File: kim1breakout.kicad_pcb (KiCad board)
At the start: 2 copper layers, 110 x 90.7 mm, 3 parts, among them J1 Conn_01x44, J2 Conn_01x44, J3 Conn_02x22_Top_Bottom

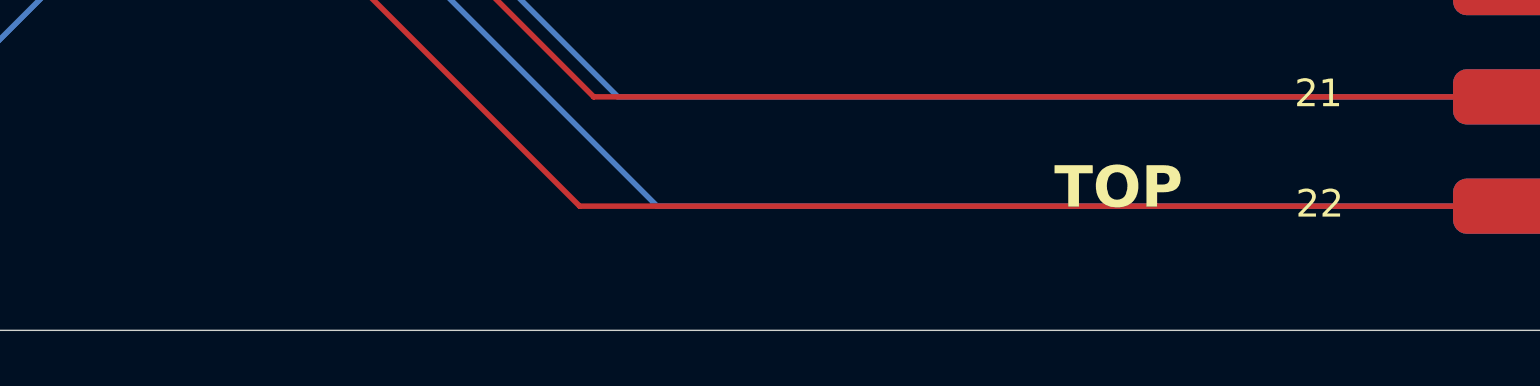
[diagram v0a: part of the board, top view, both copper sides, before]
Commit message: Add pointer to Github repo to the PCB
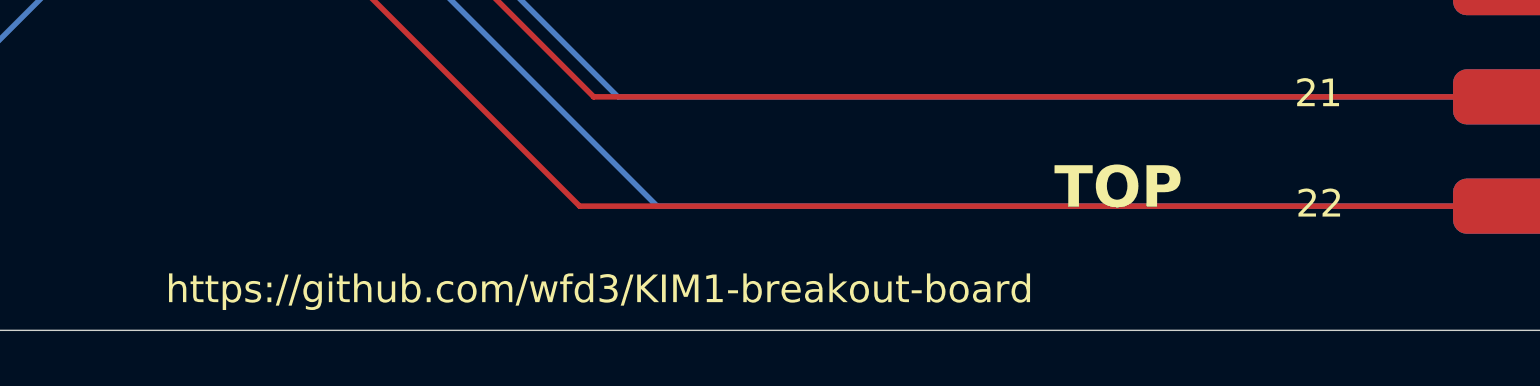
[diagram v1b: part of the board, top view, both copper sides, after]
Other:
- board text added: "https://github.com/wfd3/KIM1-breakout-board"
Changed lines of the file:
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@@
+		)
+	)
+	(gr_text "https://github.com/wfd3/KIM1-breakout-board"
+		(at 153.5 143.5 0)
+		(layer "F.SilkS")
+		(effects
+			(font
+				(size 1 1)
+				(thickness 0.1)
+			)
+			(justify left bottom)
 		)
 	)

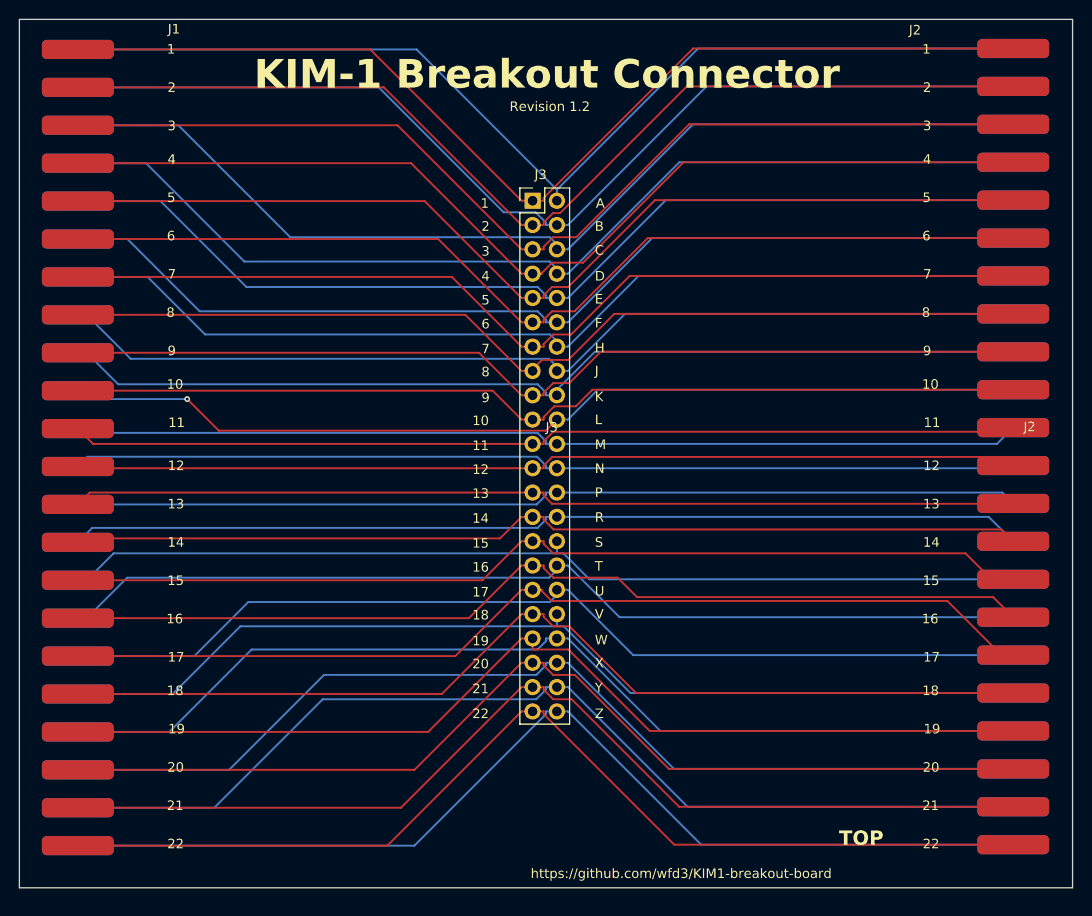
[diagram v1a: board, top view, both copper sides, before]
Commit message: Update artwork, shrink board
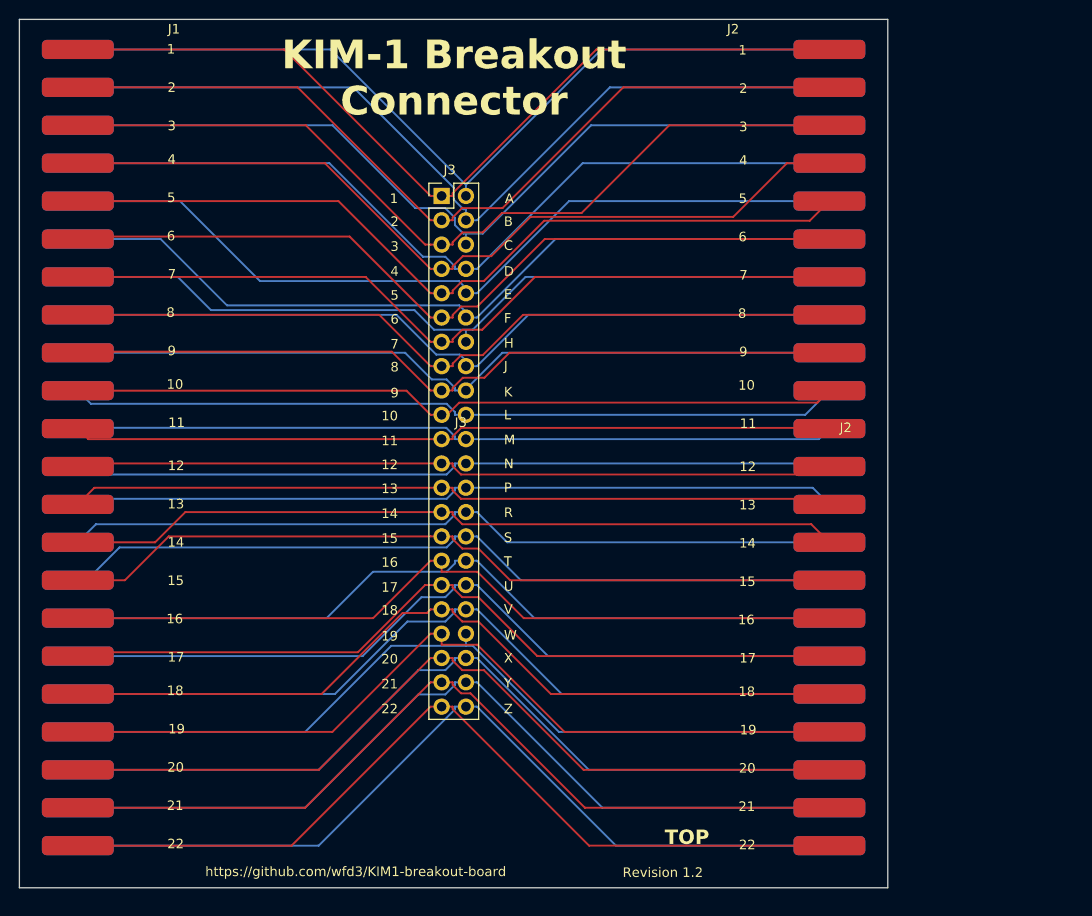
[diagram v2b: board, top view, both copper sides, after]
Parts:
- moved J2 19.2 mm to (188.8, 97.5)
- moved J3 9.51 mm to (146.2, 96.3)
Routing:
- net Net-(J1-Pin_32): track 101.2 -> 80.8 mm, vias 1 -> 0
- net Net-(J1-Pin_31): track 102.2 -> 82.1 mm
- net Net-(J1-Pin_26): track 107.8 -> 87.8 mm
- net Net-(J1-Pin_29): track 104.3 -> 84.3 mm
- net Net-(J1-Pin_10): track 100.4 -> 80.6 mm
- net Net-(J1-Pin_3): track 108.6 -> 89.0 mm
- net Net-(J1-Pin_7): track 103.9 -> 84.3 mm
- net Net-(J1-Pin_5): track 106.3 -> 86.6 mm
- net Net-(J1-Pin_23): track 111.0 -> 91.4 mm
- net Net-(J1-Pin_1): track 111.0 -> 91.3 mm
- net Net-(J1-Pin_2): track 109.8 -> 90.2 mm
- net Net-(J1-Pin_8): track 102.7 -> 83.1 mm
- net Net-(J1-Pin_33): track 99.2 -> 79.7 mm
- net Net-(J1-Pin_11): track 99.2 -> 79.6 mm
- net Net-(J1-Pin_9): track 101.6 -> 82.0 mm
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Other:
- board size 110 x 90.7 mm -> 90.7 x 90.7 mm

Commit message: Widen track length to compensate for ground net resistance, update README and gerbers/
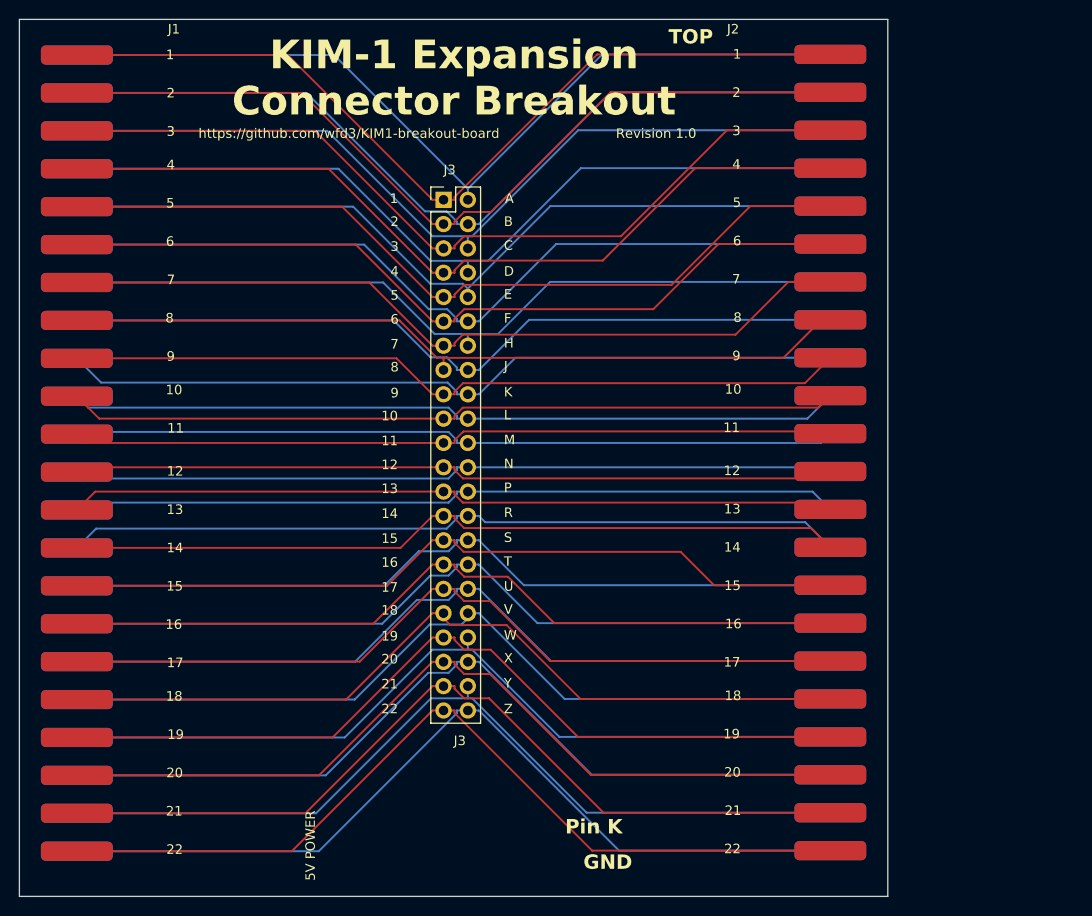
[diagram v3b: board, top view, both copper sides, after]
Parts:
- J1: footprint kim1_connectors:edge_connector_pcb_02x22_left -> kim1-connectors:pcb_slot_connector_02x22_left
- J2: footprint kim1_connectors:edge_connector_pcb_02x22_right -> kim1-connectors:pcb_slot_connector_02x22_right
- J3: footprint kim1_connectors:PinHeader_02x22_P2.54mm_Vertically_Numbered -> kim1-connectors:PinHeader_2x22_P2.54_Vertical_KIM1
- moved J3 33.2 mm to (146.1, 129.5)
- moved J2 8.71 mm to (180.1, 97.2)
- moved J1 1.43 mm to (108.9, 97.2)
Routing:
- net Net-(J1-Pin_A): track 0.00 -> 91.4 mm
- net Net-(J1-Pin_24): track 91.4 -> 0.00 mm
- net Net-(J1-Pin_23): track 91.4 -> 0.00 mm
- net Net-(J1-Pin_Z): track 0.00 -> 91.0 mm
- net Net-(J1-Pin_44): track 90.7 -> 0.00 mm
- net Net-(J1-Pin_B): track 0.00 -> 90.2 mm
- net Net-(J1-Pin_Y): track 0.00 -> 89.9 mm
- net Net-(J1-Pin_43): track 89.5 -> 0.00 mm
- net Net-(J1-Pin_25): track 89.5 -> 0.00 mm
- net Net-(J1-Pin_C): track 0.00 -> 89.1 mm
- net Net-(J1-Pin_X): track 0.00 -> 88.7 mm
- net Net-(J1-Pin_42): track 88.3 -> 0.00 mm
- net Net-(J1-Pin_D): track 0.00 -> 87.9 mm
- net Net-(J1-Pin_26): track 87.8 -> 0.00 mm
- net Net-(J1-Pin_W): track 0.00 -> 87.5 mm
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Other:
- board size 90.7 x 90.7 mm -> 90.7 x 91.6 mm
- board text added: "5V POWER"
- board text added: "GND"
- board text added: "KIM-1 Expansion Connector Breakout"
- board text added: "Pin K"
- board text added: "Revision 1.0"
- board text removed: "KIM-1 Breakout Connector"
- board text removed: "Revision 1.2"
